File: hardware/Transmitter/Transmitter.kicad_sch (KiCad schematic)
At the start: 54 parts, among them IC1 ESP32-C3-MINI-1-N4, IC1 XC6194AA03ER-G, J2 USB_C, J3 Battery, Q1 2N7002, U1 AZ1117-3.3, U2 TPS22810DRV

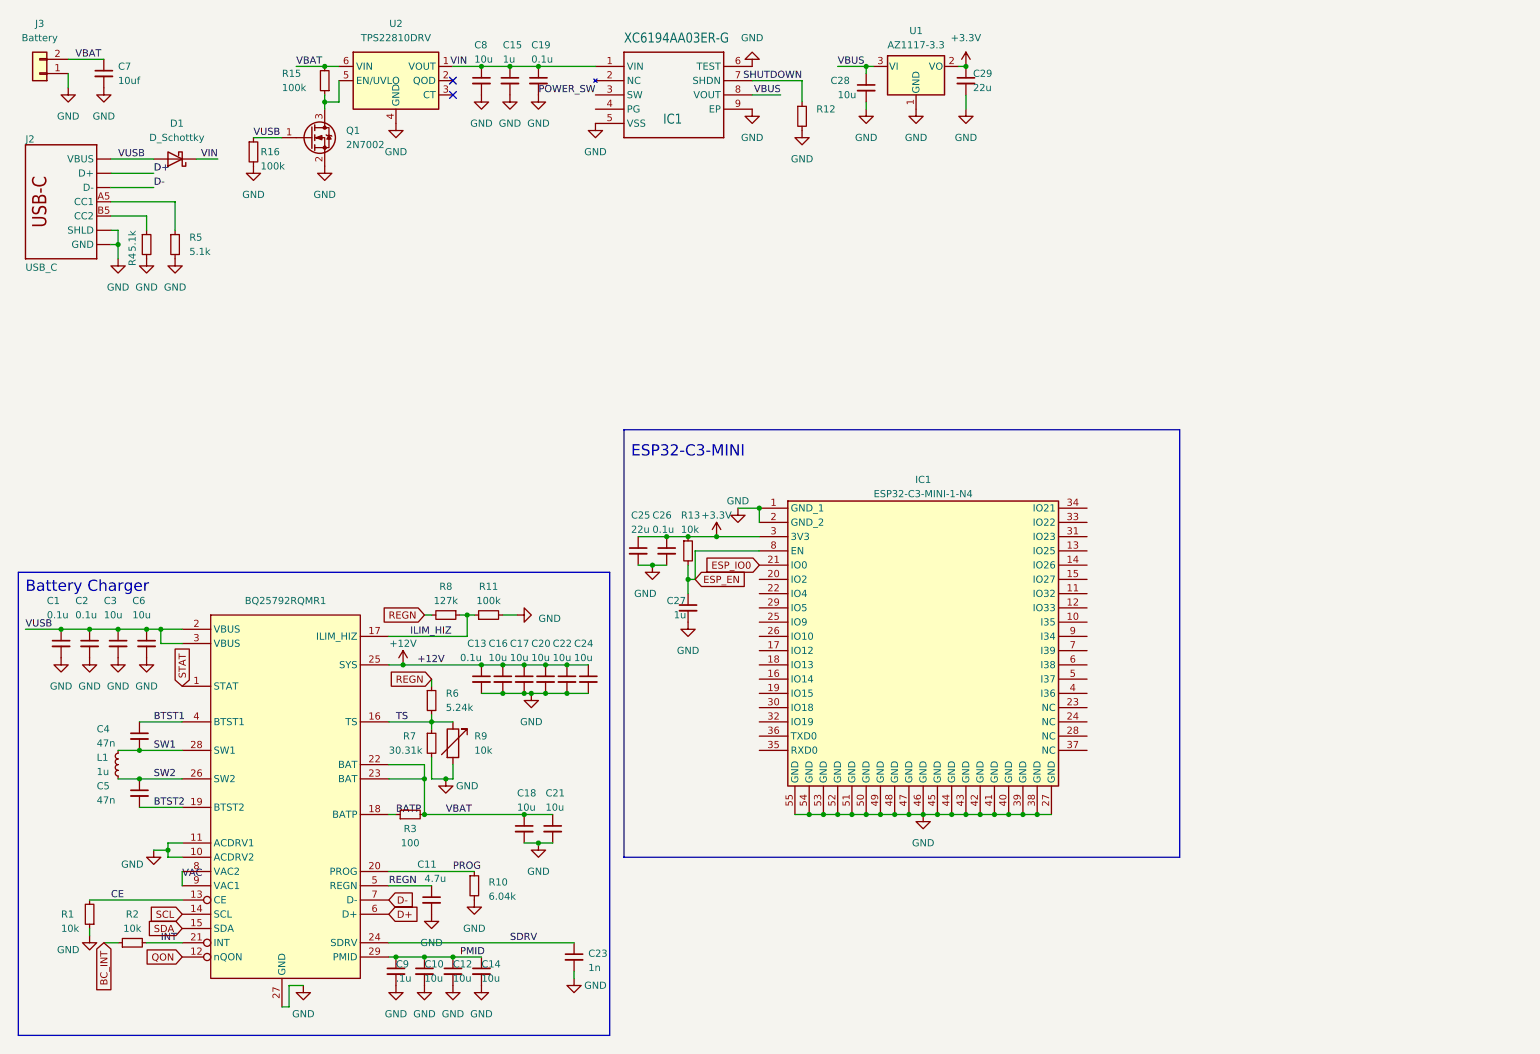
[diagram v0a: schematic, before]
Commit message: Completed Transmitter Schematic
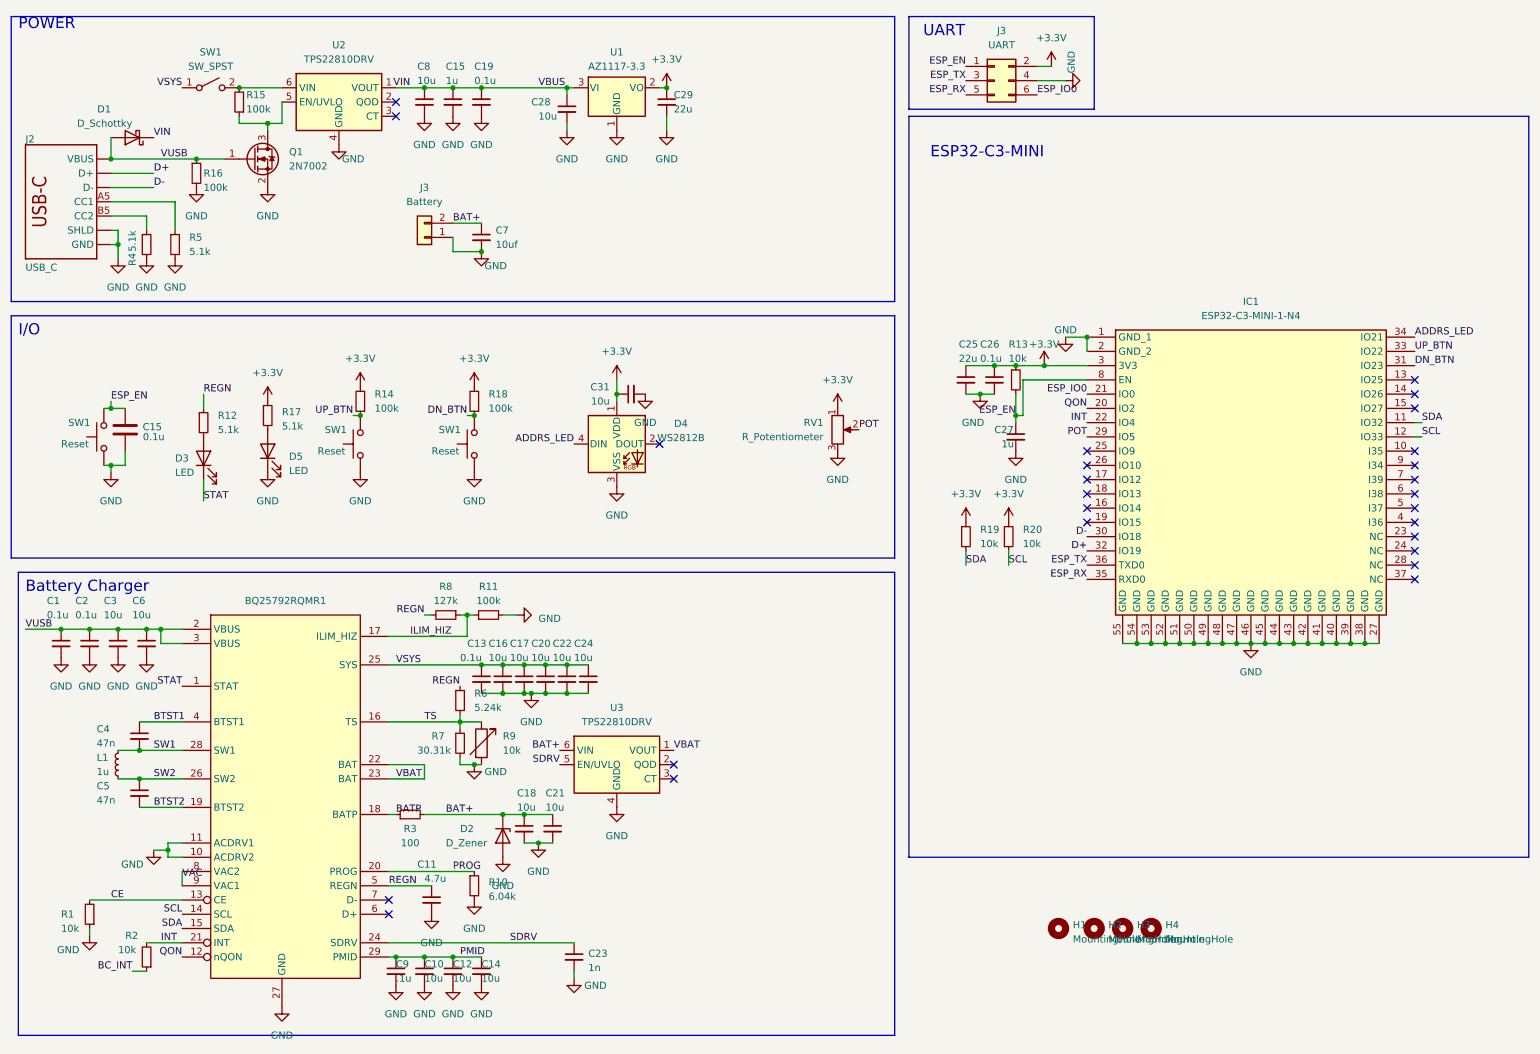
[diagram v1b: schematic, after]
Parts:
- removed IC1: XC6194AA03ER-G, XC6194BANNERG, symbol xc6194c-eagle-import:XC6194A310ER-G
- added C15: 0.1u, Capacitor_SMD:C_0402_1005Metric, symbol Device:C
- added C31: 10u, Capacitor_SMD:C_0603_1608Metric, symbol Device:C_Small
- added D2: D_Zener, symbol Device:D_Zener
- added D3: LED, symbol Device:LED
- added D4: WS2812B, LED_SMD:LED_WS2812B_PLCC4_5.0x5.0mm_P3.2mm, symbol LED:WS2812B
- added D5: LED, Capacitor_SMD:C_0805_2012Metric, symbol Device:LED
- added H1, H2, H3, H4: MountingHole, MountingHole:MountingHole_2.2mm_M2, symbol Mechanical:MountingHole
- added J3: UART, Connector_PinHeader_1.27mm:PinHeader_2x03_P1.27mm_Vertical_SMD, symbol Connector_Generic:Conn_02x03_Odd_Even
- added R14, R18: 100k, symbol Device:R_Small
- added R17: 5.1k, Resistor_SMD:R_0402_1005Metric, symbol Device:R_Small
- added R19, R20: 10k, symbol Device:R_Small
- added RV1: R_Potentiometer, symbol Device:R_Potentiometer
- added SW1 (x3): Reset, Switch:Tactile_5.5mmx2.85mm, symbol Switch:SW_Push
- added SW1: SW_SPST, symbol Switch:SW_SPST
- added U3: TPS22810DRV, Package_SON:WSON-6-1EP_2x2mm_P0.65mm_EP1x1.6mm, symbol Power_Management:TPS22810DRV
- R12: value R_Small -> 5.1k
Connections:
- net SHUTDOWN is gone; now on net REGN: R12.1
- net VIN is gone; now on net VBUS: C15.1, C19.1, C8.1, D1.1 (K), U2.1 (VOUT)
- net +3.3V: now also C31.1, D4.1 (VDD), J3.2 (Pin_2), R14.2, R17.1, R18.2, R19.1, R20.1, RV1.1
- net D+: now also IC1.32 (IO19); no longer BQ25792RQMR1.6 (D+)
- net D-: now also IC1.30 (IO18); no longer BQ25792RQMR1.7 (D-)
- net ESP_EN: now also C15.1, J3.1 (Pin_1), SW1.2
- net ESP_IO0: now also J3.6 (Pin_6)
- net GND: now also C15.2, C31.2, D2.2 (A), D4.3 (VSS), D5.1 (K), J3.4 (Pin_4), RV1.3, SW1.1, SW1.1, SW1.1, U3.4 (GND), U3.7 (GND); no longer R12.2
- net INT: now also IC1.22 (IO4)
- net QON: now also IC1.20 (IO2)
- net SCL: now also IC1.12 (IO33), R20.2
- net SDA: now also IC1.11 (IO32), R19.2
- net SDRV: now also U3.5 (EN/UVLO)
- net STAT: now also D3.1 (K)
- net VBAT: now also U3.1 (VOUT); no longer C18.1, C21.1, C7.1, J3.2 (Pin_2), R15.2, R3.2, U2.6 (VIN)
- net POT: now reaches IC1.29 (IO5)
- net POT: now also RV1.2
- net DN_BTN: now reaches IC1.31 (IO23)
- net DN_BTN: now also R18.1, SW1.2
- net UP_BTN: now reaches IC1.33 (IO22)
- net UP_BTN: now also R14.1, SW1.2
- net ADDRS_LED: now reaches IC1.34 (IO21)
- net ADDRS_LED: now also D4.4 (DIN)
- net ESP_RX: now reaches IC1.35 (RXD0)
- net ESP_RX: now also J3.5 (Pin_5)
- net ESP_TX: now reaches IC1.36 (TXD0)
- net ESP_TX: now also J3.3 (Pin_3)
- net +12V renamed VSYS
- net VSYS: now also SW1.1 (A)
- new net: R15.2, SW1.2 (B), U2.6 (VIN)
- new net: D3.2 (A), R12.2
- new net: D5.2 (A), R17.2
- new net BAT+: C18.1, C21.1, C7.1, D2.1 (K), J3.2 (Pin_2), R3.2, U3.6 (VIN)
- no-connect marks 2 -> 26
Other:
- note added: "I/O"
- note added: "POWER"
- note added: "UART"
- moved on the sheet: C15, C19, C25, C26, C27, C28, C29, C7, C8, D1, IC1, J3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

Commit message: Transmitter PCB complete
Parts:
- removed C1: 0.1u, Capacitor_SMD:C_0402_1005Metric, symbol Device:C_Small
- removed J2: USB_C, USB-C-16P-LESSPASTE-2, symbol TinyS3_P3-eagle-import:USB_C
- removed SW1 (x2): Reset, Switch:Tactile_5.5mmx2.85mm, symbol Switch:SW_Push
- added H1: MountingHole, MountingHole:MountingHole_2.2mm_M2, symbol Mechanical:MountingHole
- added J1: USB_C_Receptacle_USB2.0, footprints:CONN_GSB1CA11101DSHR_AMP, symbol Connector:USB_C_Receptacle_USB2.0
- added J2: UP_BTN, Connector_JST:JST_PH_B2B-PH-K_1x02_P2.00mm_Vertical, symbol Connector_Generic:Conn_01x02
- added J4: Conn_01x03, Connector_JST:JST_PH_B3B-PH-K_1x03_P2.00mm_Vertical, symbol Connector_Generic:Conn_01x03
- C17: renamed from C8; footprint (none) -> Capacitor_SMD:C_0402_1005Metric
- C21: renamed from C15; footprint (none) -> Capacitor_SMD:C_0402_1005Metric
- C24: renamed from C19; footprint (none) -> Capacitor_SMD:C_0402_1005Metric
- C25: renamed from C7; footprint (none) -> Capacitor_SMD:C_0402_1005Metric
- C27: renamed from C28; footprint (none) -> Capacitor_SMD:C_0402_1005Metric
- C28: renamed from C29; footprint (none) -> Capacitor_SMD:C_0402_1005Metric
- D1: renamed from D3; footprint (none) -> LED_SMD:LED_0603_1608Metric
- D3: renamed from D1; footprint (none) -> Diode_SMD:D_SOD-128
- D4: renamed from D2; footprint (none) -> Diode_SMD:D_SOD-323F
- J3: value Battery -> DN_BTN; footprint (none) -> Connector_JST:JST_PH_B2B-PH-K_1x02_P2.00mm_Vertical
- J3: footprint Connector_PinHeader_1.27mm:PinHeader_2x03_P1.27mm_Vertical_SMD -> Connector_PinHeader_1.27mm:PinHeader_2x03_P1.27mm_Vertical
- R14: renamed from R18; footprint (none) -> Capacitor_SMD:C_0402_1005Metric
- R18: renamed from R19; footprint (none) -> Capacitor_SMD:C_0402_1005Metric
- R19: renamed from R20; footprint (none) -> Capacitor_SMD:C_0402_1005Metric
- R3: renamed from R4; footprint (none) -> Capacitor_SMD:C_0402_1005Metric
- R4: renamed from R5; footprint (none) -> Capacitor_SMD:C_0402_1005Metric
- R5: renamed from R12; footprint (none) -> Capacitor_SMD:C_0402_1005Metric
- R7: renamed from R16; footprint (none) -> Capacitor_SMD:C_0402_1005Metric
- R8: renamed from R15; footprint (none) -> Capacitor_SMD:C_0402_1005Metric
- R9: renamed from R14; footprint (none) -> Capacitor_SMD:C_0402_1005Metric
- RV1: footprint (none) -> Potentiometer_THT:Potentiometer_Alps_RK09L_Single_Vertical
- SW2: renamed from SW1; footprint (none) -> Connector_JST:JST_PH_B2B-PH-K_1x02_P2.00mm_Vertical
- U3: renamed from U1; footprint (none) -> AZ1117:SOT223
- renumbered C11 to C10, C12 to C11, C13 to C12, C14 to C13, C16 to C14, C17 to C15, C18 to C16, C20 to C18, C21 to C19, C22 to C20, C23 to C22, C24 to C23, C31 to C26, C25 to C29, C26 to C30, C27 to C31, C4 to C5, C5 to C6, C6 to C7, C9 to C8, C10 to C9, D5 to D2, D4 to D5, H1 to H2, H2 to H3, H3 to H4, H4 to H5, R3 to R10, R8 to R11, R6 to R12, R7 to R13, R10 to R15, R9 to R16, R11 to R17, R13 to R20, R17 to R6, U2 to U1, U3 to U2
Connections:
- net BAT+: now also J4.3 (Pin_3); no longer J3.2 (Pin_2)
- net BC_INT: now also IC1.22 (IO4)
- net D+: now also J1.A6 (D+), J1.B6 (D+)
- net D-: now also J1.A7 (D-), J1.B7 (D-)
- net DN_BTN: now also IC1.10 (I35), J3.2 (Pin_2); no longer IC1.31 (IO23)
- net GND: now also U3.4 (GND), J1.A1 (GND), J1.A12 (GND), J1.B1 (GND), J1.B12 (GND), J2.1 (Pin_1), J4.1 (Pin_1)
- net INT: no longer IC1.22 (IO4)
- net POT: now also IC1.14 (IO26); no longer IC1.29 (IO5)
- net SCL: now also IC1.19 (IO15); no longer IC1.12 (IO33)
- net SDA: now also IC1.18 (IO13); no longer IC1.11 (IO32)
- net UP_BTN: now also IC1.9 (I34), J2.2 (Pin_2); no longer IC1.33 (IO22)
- net VUSB: now also J1.A4 (VBUS), J1.A9 (VBUS), J1.B4 (VBUS), J1.B9 (VBUS)
- net at R4.1: now also J1.B5 (CC2)
- net at R3.1: now also J1.A5 (CC1)
- no-connect marks 26 -> 25
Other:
- moved on the sheet: C17, C21, C24, C25, C27, C28, D3, Q1, R3, R4, R7, R8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

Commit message: Removed old files
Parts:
- added J6: JST_PH, Connector_JST:JST_PH_B6B-PH-K_1x06_P2.00mm_Vertical, symbol Connector_Generic:Conn_01x06
- added Q10, Q11, Q2, Q3, Q4, Q8, Q9: NChan, Package_TO_SOT_SMD:SOT-23, symbol Transistor_FET:DMG3418L
- added Q5, Q6, Q7: PChan, Package_TO_SOT_SMD:SOT-23, symbol Transistor_FET:BSS83P
- added R21, R22, R23, R24, R25, R26, R28, R30, R32: 100k, Resistor_SMD:R_0402_1005Metric, symbol Device:R_Small
- added R27: 282k, Resistor_SMD:R_0402_1005Metric, symbol Device:R_Small
- added R29: 155k, Resistor_SMD:R_0402_1005Metric, symbol Device:R_Small
- added R31: 28k, Resistor_SMD:R_0402_1005Metric, symbol Device:R_Small
- added R33, R34, R35, R36: 400, Resistor_SMD:R_2010_5025Metric, symbol Device:R_Small
- renumbered C2 to C1, C11 to C10, C12 to C11, C13 to C12, C14 to C13, C15 to C14, C16 to C15, C17 to C16, C18 to C17, C19 to C18, C20 to C19, C3 to C2, C21 to C20, C22 to C21, C23 to C22, C24 to C23, C25 to C24, C26 to C25, C27 to C26, C28 to C27, C29 to C28, C30 to C29, C31 to C30, C5 to C4, C6 to C5, C7 to C6, C8 to C7, C9 to C8, C10 to C9
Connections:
- net GND: now also J6.1 (Pin_1), Q11.2 (S), Q2.2 (S), Q3.2 (S), Q4.2 (S), R21.2, R22.2, R23.2, R28.2, R30.2, R32.2
- net M3: now reaches IC1.11 (IO32)
- net M3: now also Q3.1 (G), R22.1
- net S3: now reaches IC1.12 (IO33)
- net S3: now also R29.2, R30.1
- net S2: now reaches IC1.13 (IO25)
- net S2: now also R27.2, R28.1
- net C3: now reaches IC1.15 (IO27)
- net C3: now also Q10.1 (G)
- net C1: now reaches IC1.16 (IO14)
- net C1: now also Q8.1 (G)
- net M2: now reaches IC1.31 (IO23)
- net M2: now also Q2.1 (G), R21.1
- net C2: now reaches IC1.33 (IO22)
- net C2: now also Q9.1 (G)
- net S4: now reaches IC1.5 (I37)
- net S4: now also R31.2, R32.1
- net M4: now reaches IC1.6 (I38)
- net M4: now also Q4.1 (G), R23.1
- net C4: now reaches IC1.7 (I39)
- net C4: now also Q11.1 (G)
- new net: Q10.3 (D), R35.2
- new net: Q11.3 (D), R36.2
- new net: Q6.2 (S), R29.1
- new net: Q4.3 (D), Q7.1 (G), R26.2
- new net: Q7.2 (S), R31.1
- new net: Q8.3 (D), R33.2
- new net: Q9.3 (D), R34.2
- new net: Q2.3 (D), Q5.1 (G), R24.2
- new net: Q3.3 (D), Q6.1 (G), R25.2
- new net: Q5.2 (S), R27.1
- new net BAT_+: J6.5 (Pin_5), R33.1
- new net BAT_A: J6.4 (Pin_4), Q5.3 (D), Q8.2 (S), R24.1, R34.1
- new net BAT_B: J6.3 (Pin_3), Q6.3 (D), Q9.2 (S), R25.1, R35.1
- new net BAT_C: J6.2 (Pin_2), Q10.2 (S), Q7.3 (D), R26.1, R36.1
- new net TC: J6.6 (Pin_6)
- no-connect marks 25 -> 19
